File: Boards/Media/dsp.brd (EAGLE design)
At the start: 160 x 100 mm, 119 parts, among them IC2 OPA2277U, IC4 OPA2277U, IC5 OPA2277U, IC6 OPA2277U, IC7 OPA2277U, IC8 OPA2277U, Y1 12.288MHz

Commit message: DSP sch nearly complete, added most components. Still needs reset generator and final check
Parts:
- removed IC8: OPA2277U, linear:SO08
- added C100, C62, C64, C65, C66, C67, C68, C70, C79, C80, C89, C90, C99: 0.1uF, 1_SparkFun-Capacitors:0603-CAP
- added C101, C102, C104, C107, C108, C109, C110, C111, C112, C61, C63, C69, C71, C81, C82, C91, C92: 10u, rcl:PANASONIC_B
- added C103, C105, C106, C72, C73, C83, C84, C93, C94: 10uF-A, 1_SparkFun-Capacitors:PANASONIC_C
- added C113, C114: 12p, 1_SparkFun-Capacitors:0603-CAP
- added C115, C116: .1u, 1_SparkFun-Capacitors:0603-CAP
- added C74, C75, C85, C86, C95, C96: 1n, 1_SparkFun-Capacitors:0603-CAP
- added C76, C77, C78, C87, C88, C97, C98: 100p, 1_SparkFun-Capacitors:0603-CAP
- added JP10: XLR Aux IN, 1_SparkFun-Connectors:MOLEX-1X3
- added JP11: DVD In, 1_SparkFun-Connectors:MOLEX-1X2
- added JP12: PC Input Stereo, 1_SparkFun-Connectors:MOLEX-1X3
- added JP13: USB Audio, 1_SparkFun-Connectors:MOLEX-1X4
- added JP14: RPi Audio In, 1_SparkFun-Connectors:MOLEX-1X4
- added R26, R27, R28, R29, R30, R31, R32, R33: (no value), 1_SparkFun-Resistors:1206
- added R34, R35, R36, R37, R42, R43, R48, R49: 200, 1_SparkFun-Resistors:1206
- added R38, R39, R40, R41, R44, R45, R46, R47, R50, R51, R52, R53, R54, R55, R56: 4.7K, 1_SparkFun-Resistors:1206
- added R57, R61: 1M, 1_SparkFun-Resistors:1206
- added R58, R59: 22, 1_SparkFun-Resistors:1206
- added R60: 1.5K, 1_SparkFun-Resistors:1206
- added TP4: VOUT-L, 1_SparkFun-Passives:PAD.03X.03
- added TP5: VOUT-R, 1_SparkFun-Passives:PAD.03X.03
- added TP6: VIN-L, 1_SparkFun-Passives:PAD.03X.03
- added TP7: VIN-R, 1_SparkFun-Passives:PAD.03X.03
- added TP8: Suspend, 1_SparkFun-Passives:PAD.03X.03
- added U$35, U$38, U$39: LME49724, 0_DSP:SOIC-8
- added U$40: PCM2903, 0_DSP:SSOP-28
- added U$43: 74AHC1G08, 1_SparkFun-DigitalIC:SOT23-5
- added Y2: 12MHz, 1_SparkFun-FreqCtrl:HC49U-V
- C12, C17, C18, C28, C32, C39, C40, C43, C51, C52, C53, C54: device 1_SparkFun-Capacitors:CPOL-RADIAL-10UF-25V -> rcl:PANASONIC_B
- C29: value 100uF -> 10u; device 1_SparkFun-Capacitors:CPOL-RADIAL-100UF-25V -> rcl:PANASONIC_B
- C45: value 10u -> 0.1uF; device 1_SparkFun-Capacitors:CPOL-RADIAL-10UF-25V -> 1_SparkFun-Capacitors:0603-CAP
- C46, C47: value 220uF -> 10u; device 1_SparkFun-Capacitors:CPOL-RADIAL-100UF-25V -> rcl:PANASONIC_B
- C57: value 10u -> 10uF-A; device 1_SparkFun-Capacitors:CPOL-RADIAL-10UF-25V -> 1_SparkFun-Capacitors:PANASONIC_C
- C58: value 0.1uF -> 10uF-A; device 1_SparkFun-Capacitors:0603-CAP -> 1_SparkFun-Capacitors:PANASONIC_C
- C59: value 0.1uF -> 1n
- C60: value 10u -> 1n; device 1_SparkFun-Capacitors:CPOL-RADIAL-10UF-25V -> 1_SparkFun-Capacitors:0603-CAP
- moved C59 437.7 mm to (-22.9, 94.0)
- moved C60 437.2 mm to (-26.7, 94.0)
- moved R25 404.6 mm to (-61.0, 100.3)
- moved R24 403.7 mm to (-55.9, 100.3)
- moved R23 403.0 mm to (-50.8, 100.3)
- moved R22 402.3 mm to (-45.7, 100.3)
- moved C58 395.3 mm to (-34.3, 53.3)
- moved C56 395.1 mm to (-19.1, 94.0)
- moved C57 394.3 mm to (-27.9, 53.3)
- moved C55 394.2 mm to (-15.2, 94.0)
- moved JP9 392.2 mm to (-20.3, 76.2)
- moved R21 347.7 mm to (-40.6, 100.3)
- moved R20 347.0 mm to (-35.6, 100.3)
- moved R19 346.4 mm to (-30.5, 100.3)
- moved R18 345.9 mm to (-25.4, 100.3)
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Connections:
- new net N$100: R59.2, U$40.2
- new net N$101: R55.1, R56.1
- new net N$102: JP13.2, R59.1
- new net N$103: R60.2, U$43.4
- new net N$104: C113.2, R61.2, U$40.21, Y2.2
- new net N$105: TP8.P$1, U$40.28
- new net N$106: C114.2, R61.1, U$40.20, Y2.1
- new net N$107: C115.2, U$40.24
- new net N$108: C116.2, U$40.25
- new net N$37: C73.+, R33.1, U$39.5
- new net N$48: C72.+, R32.1, U$39.4
- new net N$50: R24.1, R27.2, U$35.1
- new net N$51: R23.1, R28.1, U$38.8
- new net N$53: C67.1, U$39.2
- new net N$54: C72.-, R34.2
- new net N$55: C73.-, R35.2
- new net N$56: C57.+, R36.2
- new net N$57: R30.2, R32.2, U$39.8
- new net N$58: JP10.3, R30.1
- new net N$59: JP10.1, R31.1
- new net N$60: R31.2, R33.2, U$39.1
- new net N$61: C75.2, C76.2, R35.1, U$17.54
- new net N$62: C58.+, R37.2
- new net N$63: C74.1, C76.1, R34.1, U$17.53
- new net N$64: C60.2, C77.2, R37.1, U$17.56
- new net N$65: C59.1, C77.1, R36.1, U$17.55
- new net N$66: C58.-, IC5.1, R38.2
- new net N$67: C57.-, IC5.7, R39.2, R41.2
- new net N$68: IC5.2, R38.1, R39.1
- new net N$69: IC5.6, R40.2, R41.1
- new net N$70: C106.-, JP11.1
- new net N$71: C83.+, R42.2
- new net N$72: C86.2, C87.2, R43.1, U$17.58
- new net N$73: C85.1, C87.1, R42.1, U$17.57
- new net N$74: C84.+, R43.2
- new net N$75: C83.-, IC6.7, R45.2, R47.2
- new net N$76: C84.-, IC6.1, R44.2
- new net N$77: IC6.2, R44.1, R45.1
- new net N$78: IC6.6, R46.2, R47.1
- new net N$79: C103.+, C88.1, R46.1
- new net N$80: C93.+, R48.2
- new net N$81: C96.2, C97.2, R49.1, U$17.60
- new net N$82: C95.1, C97.1, R48.1
- new net N$83: C94.+, R49.2
- new net N$84: C93.-, IC7.7, R51.2, R53.2
- new net N$85: C94.-, IC7.1, R50.2
- new net N$86: IC7.2, R50.1, R51.1
- new net N$87: IC7.6, R52.2, R53.1
- new net N$88: C105.+, C98.1, R52.1
- new net N$89: C103.-, JP12.1
- new net N$90: U$17.59
- new net N$91: C105.-, JP12.3
- new net N$92: C106.+, C78.1, R40.1
- new net N$93: TP4.P$1, U$40.16
- new net N$94: TP5.P$1, U$40.15
- new net N$95: TP6.P$1, U$40.12
- new net N$96: TP7.P$1, U$40.13
- new net N$97: JP13.3, R58.1, R60.1
- new net N$98: R58.2, U$40.1
- new net N$99: R54.2, R55.2, U$43.2
- new net VBUS: JP13.4, R54.1, R57.2, U$40.9
- net 3.3V_A: now also C104.+, C18.+, C28.+, C43.+; no longer C28.1, C39.1, C43.1, C45.1
- net 3V3_D: now also C107.+, C108.+, C109.+, C110.+, C111.+, C112.+, C17.+, C40.+, C45.2, U$40.10, U$40.14, U$40.17, U$40.19, U$40.23, U$40.27, U$40.3, U$40.8, U$43.1, U$43.5; no longer C12.1, C32.1
- net BCLK2: now also U$17.28
- net BCLK3: now also JP14.1
- net BCLK_OUT1: now also U$17.21
- net CLOCK: now also U$17.2
- net DATA2: now also U$17.27
- net DATA3: now also JP14.3
- net DATA_OUT1: now also U$17.20
- net FILTER: now also C39.+; no longer C40.1
- net GND: now also C100.2, C101.-, C102.-, C104.-, C107.-, C108.-, C109.-, C110.-, C111.-, C112.-, C113.1, C114.1, C12.-, C17.-, C18.-, C28.-, C29.-, C32.-, C39.-, C40.-, C43.-, C45.1, C46.-, C47.-, C51.+, C52.+, C53.-, C54.+, C59.2, C61.-, C62.1, C63.+, C64.1, C65.2, C66.2, C67.2, C68.2, C69.-, C70.2, C71.+, C74.2, C75.1, C78.2, C79.1, C80.2, C81.+, C82.+, C85.2, C86.1, C88.2, C89.1, C90.2, C91.+, C92.-, C95.2, C96.1, C98.2, C99.1, IC5.3, IC5.5, IC6.3, IC6.5, IC7.3, IC7.5, JP10.2, JP11.2, JP12.2, JP13.1, JP14.4, R56.2, R57.1, U$35.7, U$38.7, U$39.7, U$40.11, U$40.18, U$40.22, U$40.26, U$40.4, U$43.3; no longer C12.2, C17.2, C18.2, C28.2, C29.1, C32.2, C39.2, C40.2, C43.2, C45.2, C46.2, C47.1, C51.2, C52.1, C53.2, C54.1, C57.2, C58.2, C59.1
- net LRCLK2: now also U$17.29
- net LRCLK3: now also JP14.2
- net LRCLK_OUT1: now also U$17.22
- net N$17: now also C29.+; no longer C29.2
- net N$38: now also JP9.1, R28.2, U$38.4; no longer IC6.3, U$17.42
- net N$39: now also JP9.3, R29.2, U$38.5; no longer IC6.5, U$17.43
- net N$4: now also C12.+; no longer C18.1
- net N$40: now also JP8.1, R26.1, U$35.4; no longer IC5.3, U$17.40
- net N$41: now also JP8.3, R27.1, U$35.5; no longer IC5.5, U$17.41
- net N$42: now also R24.2, U$17.41; no longer IC5.1, IC5.2, R22.1
- net N$43: now also C66.1, U$35.2; no longer IC5.6, IC5.7, R23.1
- net N$44: now also C65.1, U$38.2; no longer IC6.1, IC6.2, R24.1
- net N$45: now also R25.2, U$17.40; no longer IC6.6, IC6.7, R25.1
- net N$46: now also R23.2, U$17.42; no longer JP8.1, R22.2
- net N$47: now also R22.2, U$17.43; no longer JP8.3, R23.2
- net N$49: now also R25.1, R26.2, U$35.8; no longer JP9.1, R24.2
- net N$52: now also R22.1, R29.1, U$38.1; no longer JP9.3, R25.2
- net N$7: now also C32.+; no longer C17.1
- net SPDIF-OUT: now also C115.1
- net SPDIFIN: now also C116.1
- net VCC: now also C101.+, C102.+, C46.+, C47.+, C53.+, C61.+, C62.2, C68.1, C69.+, C79.2, C89.2, C92.+, C99.2, U$35.3, U$38.3, U$39.3; no longer C46.1, C51.1, C53.1, C57.1, C58.1, IC8.8
- net VNEG: now also C100.1, C51.-, C52.-, C54.-, C63.-, C64.2, C70.1, C71.-, C80.1, C81.-, C82.-, C90.1, C91.-, U$35.6, U$38.6, U$39.6; no longer C47.2, C52.2, C54.2, C59.2, C60.2, IC8.4
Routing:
- net GND: track 91.4 -> 0.00 mm, vias 3 -> 0
- net VCC: track 29.3 -> 0.00 mm

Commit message: Began laying out DSP board
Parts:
- removed C108, C109, C111, C51, C61, C63, C69, C71, C91, C92: 10u, rcl:PANASONIC_B
- removed JP2: (no value), 1_SparkFun-Connectors:1X04
- removed TP1: FM antenna, 1_SparkFun-Passives:PAD.03X.03
- added C117: 0.1u, 1_SparkFun-Capacitors:0603-CAP
- added JP15: FM Antenna, 1_SparkFun-Connectors:1X02
- added R62: 10K, 1_SparkFun-Resistors:1206
- added S1: (no value), 1_SparkFun-Electromechanical:TACTILE-PTH
- added U$52: TLV803, 0_DSP:SOT23
- C47: value 10u -> 0.1uF; device rcl:PANASONIC_B -> 1_SparkFun-Capacitors:0603-CAP
- moved C115 373.5 mm to (44.5, 46.7), turned to 90 degrees
- moved C116 372.3 mm to (42.2, 46.7), turned to 90 degrees
- moved C114 365.4 mm to (34.3, 54.4), turned to 180 degrees
- moved C113 365.2 mm to (34.3, 56.9), turned to 180 degrees
- moved JP14 356.7 mm to (26.9, 37.8), turned to 90 degrees
- moved TP8 353.4 mm to (24.6, 62.5)
- moved Y2 353.0 mm to (29.5, 54.9), turned to 90 degrees
- moved C112 343.0 mm to (16.8, 64.5), turned to 270 degrees
- moved C110 341.0 mm to (27.9, 64.8), turned to 180 degrees
- moved C107 306.3 mm to (17.5, 46.5), turned to 90 degrees
- moved C17 302.5 mm to (76.7, 49.8), turned to 180 degrees
- moved R59 298.6 mm to (12.2, 58.9)
- moved R58 298.1 mm to (12.2, 61.2)
- moved R60 295.1 mm to (11.2, 47.8)
- moved U$43 288.5 mm to (12.2, 51.8), turned to 270 degrees
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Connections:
- removed net N$24: U$17.1, U$17.16, U$17.23, U$17.24, U$17.25, U$17.33, U$17.4, U$17.44, U$17.46, U$17.48
- net !RESET: now also R62.1, S1.1, S1.2, U$52.2
- net 3V3_D: now also C117.2, C47.2, R62.2, U$52.3; no longer C108.+, C109.+, C111.+
- net FM: now also JP15.2; no longer TP1.P$1
- net GND: now also C117.1, C47.1, JP15.1, S1.3, S1.4, U$17.1, U$17.16, U$17.23, U$17.24, U$17.25, U$17.33, U$17.4, U$17.44, U$17.46, U$17.48, U$52.1; no longer C108.-, C109.-, C111.-, C47.-, C51.+, C61.-, C63.+, C69.-, C71.+, C91.+, C92.-
- net N$102: now also JP13.3; no longer JP13.2
- net N$11: no longer JP2.1
- net N$14: no longer JP2.2
- net N$15: no longer JP2.3
- net N$16: no longer JP2.4
- net N$97: now also JP13.2; no longer JP13.3
- net VCC: no longer C47.+, C61.+, C69.+, C92.+
- net VNEG: no longer C51.-, C63.-, C71.-, C91.-
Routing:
- net GND: track 0.00 -> 141.1 mm, vias 0 -> 45
- net SCL: track 0.00 -> 121.0 mm, vias 0 -> 4
- net SDA: track 0.00 -> 104.2 mm, vias 0 -> 4
- net 3V3_D: track 0.00 -> 85.5 mm
- net 5V: track 0.00 -> 84.2 mm
- net !RESET: track 0.00 -> 60.3 mm
- net DATA2: track 0.00 -> 59.0 mm, vias 0 -> 2
- net BCLK2: track 0.00 -> 58.4 mm, vias 0 -> 2
- net LRCLK2: track 0.00 -> 57.1 mm, vias 0 -> 2
- net DATA_OUT1: track 0.00 -> 52.5 mm, vias 0 -> 2
- net 3.3V_A: track 0.00 -> 48.0 mm
- net LRCLK_OUT1: track 0.00 -> 47.6 mm, vias 0 -> 2
- net BCLK_OUT1: track 0.00 -> 46.5 mm
- net LRCLK0: track 0.00 -> 35.3 mm, vias 0 -> 1
- net DATA_OUT0: track 0.00 -> 34.9 mm, vias 0 -> 2
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- added copper zone on layer 2, net GND
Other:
- board size 160 x 100 mm -> 127 x 100 mm
- board text added: "+5V"
- board text added: "+9V"
- board text added: "-9V"
- board text added: "AM"
- board text added: "BCLK"
- board text added: "Bluetooth"
- board text added: "CTS"
- board text added: "DATA"
- board text added: "FM"
- board text added: "GND"
- board text added: "I2S In"
- board text added: "LRCLK"
- board text added: "RTS"
- board text added: "RX"
- board text added: "Radio"
- board text added: "SCL"
- board text added: "SDA"
- board text added: "SSP"
- board text added: "TX"

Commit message: DSP Board finished!
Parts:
- added LED1, LED2, LED3, LED4: (no value), 1_SparkFun-LED:LED-1206
- added R63, R64: 1K, 1_SparkFun-Resistors:1206
- added R65, R66: 160, 1_SparkFun-Resistors:1206
- moved U$35 194.7 mm to (85.1, 59.2)
- moved R28 193.8 mm to (89.4, 72.4), turned to 270 degrees
- moved R27 185.8 mm to (81.8, 53.3)
- moved R26 185.2 mm to (89.4, 65.3), turned to 90 degrees
- moved JP8 183.0 mm to (83.3, 48.8)
- moved R25 174.6 mm to (83.6, 65.3), turned to 180 degrees
- moved SJ5 171.0 mm to (79.0, 42.9), turned to 90 degrees
- moved SJ6 171.0 mm to (75.2, 42.9), turned to 90 degrees
- moved R24 168.7 mm to (80.3, 56.9), turned to 90 degrees
- moved C18 162.7 mm to (71.9, 57.4), flipped to the bottom, turned to 270 degrees
- moved C80 161.2 mm to (58.2, 91.9)
- moved C77 160.7 mm to (67.1, 72.6), turned to 180 degrees
- moved C76 160.2 mm to (70.6, 74.2), turned to 180 degrees
- moved R23 159.8 mm to (80.0, 71.9), turned to 180 degrees
- moved C66 159.0 mm to (87.6, 53.6), flipped to the bottom, turned to 180 degrees
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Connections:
- removed net N$90: U$17.59
- new net N$110: LED3.A, R63.2
- new net N$111: LED4.A, R64.2
- new net N$112: LED1.A, R66.2
- new net N$113: LED2.A, R65.2
- net 3.3V_A: now also R65.1
- net 3V3_D: now also R66.1
- net GND: now also LED1.C, LED2.C, LED3.C, LED4.C
- net N$82: now also U$17.59
- net VCC: now also R63.1
- net VNEG: now also R64.1
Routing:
- net VCC: track 11.9 -> 315.0 mm, vias 0 -> 11
- net VNEG: track 10.9 -> 294.0 mm, vias 0 -> 11
- net GND: track 141.1 -> 423.6 mm, vias 45 -> 106
- net 3.3V_A: track 48.0 -> 240.1 mm, vias 0 -> 8
- net 1.0V: track 0.00 -> 90.2 mm, vias 0 -> 4
- net N$81: track 0.00 -> 64.7 mm
- net 3V3_D: track 85.5 -> 149.9 mm, vias 0 -> 22
- net N$82: track 0.00 -> 56.5 mm
- net CLOCK: track 0.00 -> 49.4 mm, vias 0 -> 2
- net N$29: track 0.00 -> 41.9 mm, vias 0 -> 2
- net N$28: track 0.00 -> 41.1 mm, vias 0 -> 2
- net N$19: track 0.00 -> 40.7 mm
- net DAC3L0: track 0.00 -> 37.6 mm
- net DAC3L1: track 0.00 -> 36.0 mm
- net N$18: track 0.00 -> 34.7 mm
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- added copper zone on layer 15, net 3V3_D
- added copper zone on layer 16, net GND
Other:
- board size 127 x 100 mm -> 92.2 x 102.3 mm
- board text added: "- G +"
- board text added: "3.3V Analog"
- board text added: "3.3V Digital"
- board text added: "A0"
- board text added: "A1"
- board text added: "Aux In"
- board text added: "Boot"
- board text added: "D+"
- board text added: "D-"
- board text added: "DVD In"
- board text added: "Dec 2014"
- board text added: "Digital DSP Audio Router"
- board text added: "H"
- board text added: "H L"
- board text added: "L"
- board text added: "L PC In R"
- board text added: "Line Out"
- board text added: "Phones"
- board text added: "R"
- board text added: "Tristan Honscheid"
- board text added: "USB"
- board text added: "VB"
- board text added: "XLR Out 1"
- board text added: "XLR Out 2"

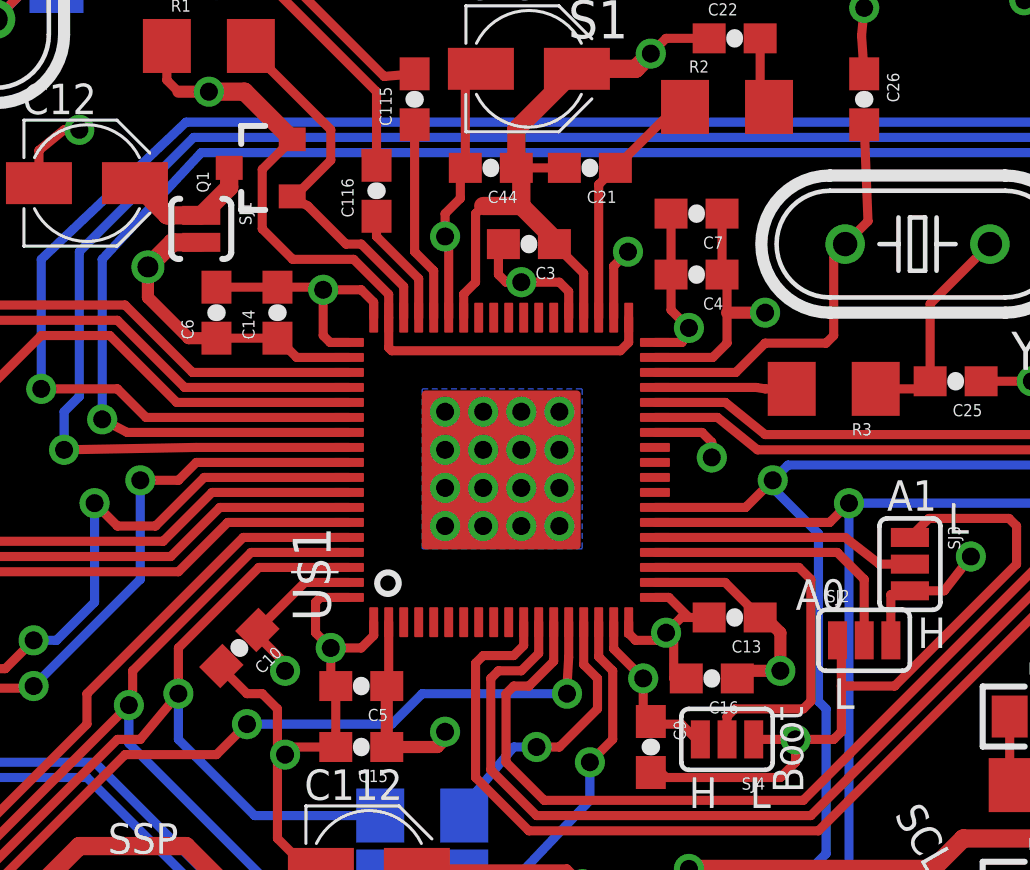
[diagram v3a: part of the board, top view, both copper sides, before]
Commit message: Final gerbers and board updates! Fixed PCB violations, now passes FreeDFM check!
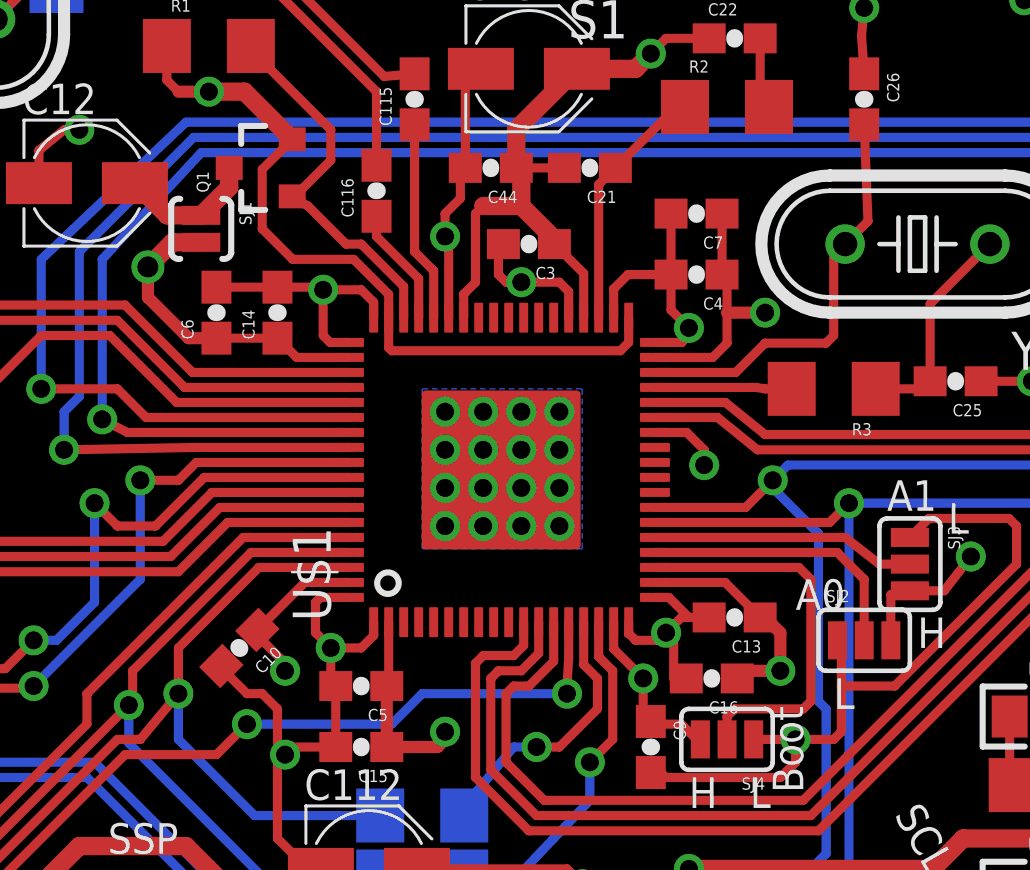
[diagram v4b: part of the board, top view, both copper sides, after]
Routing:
- net GND: track 423.6 -> 424.2 mm, vias 106 -> 105
